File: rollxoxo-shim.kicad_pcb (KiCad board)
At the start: 4 copper layers, 29 x 42 mm, 68 parts, among them J1 USB_C_Receptacle_USB2.0_14P, J2 Conn_01x02, J3 Conn_01x10, J4 Conn_01x01, J5 Conn_01x10, J6 Conn_01x03, J7 Conn_01x01, SW1 SW_Push, SW2 SW_Push, U1 SN74LV1T125DBV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

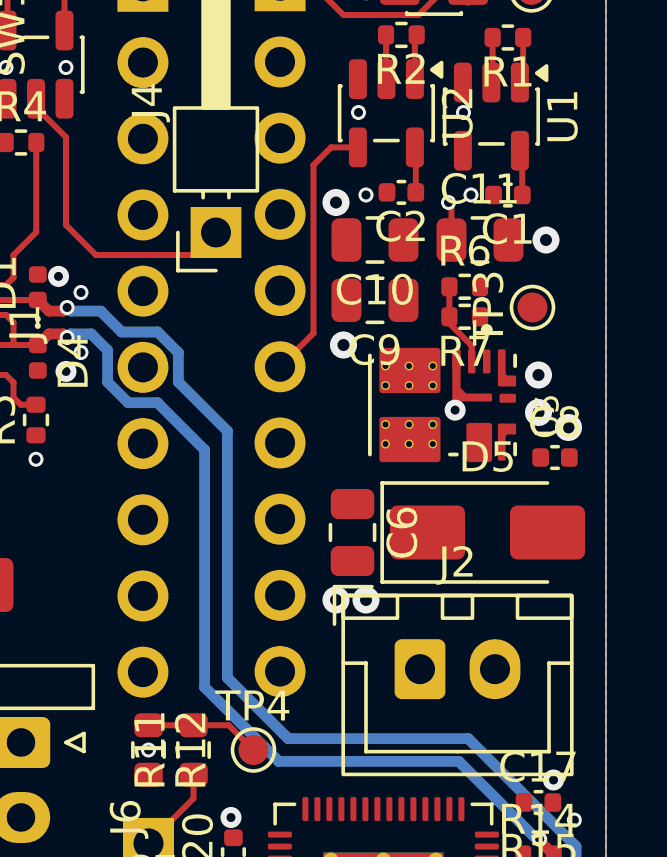
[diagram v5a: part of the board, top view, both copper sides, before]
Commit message: pcb: add power module routing
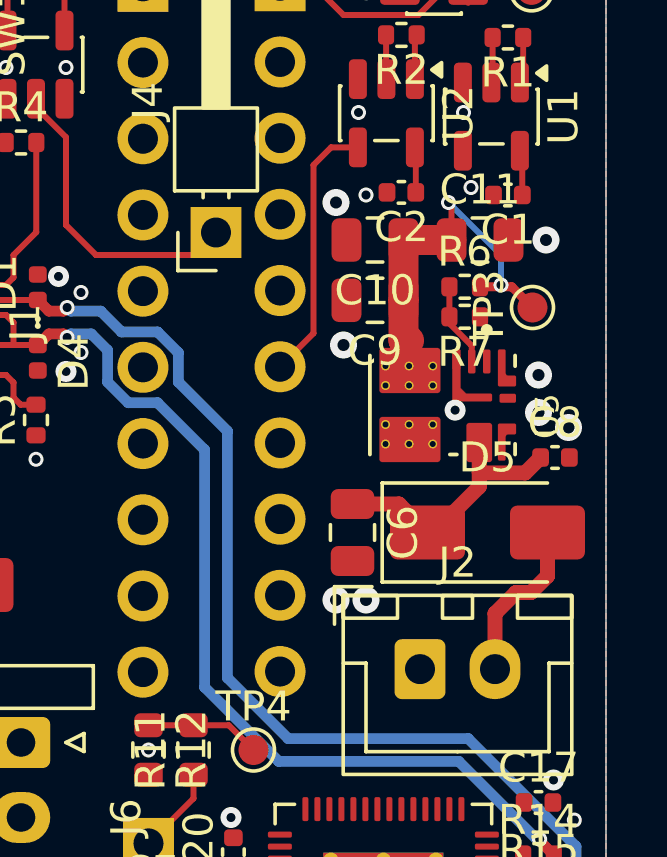
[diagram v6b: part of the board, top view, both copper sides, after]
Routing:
- net +3V3: track 7.66 -> 18.3 mm, vias 1 -> 2
- net +24V: track 0.00 -> 9.24 mm
- net Net-(D5-A): track 0.00 -> 5.57 mm
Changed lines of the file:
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@@
 	)
 	(via
-		(at 78.5 127.75)
+		(at 78.5 127.5)
 		(size 0.5)
 		(drill 0.3)
@@
 	)
 	(segment
+		(start 79.86 130.81)
+		(end 80.55 131.5)
+		(width 0.3)
+		(layer "F.Cu")
+		(net "+3V3")
+	)
+	(segment
 		(start 79.22 123.96)
 		(end 79.18 124)
@@
 	)
 	(segment
+		(start 76.25 131.26)
+		(end 76.25 132.6)
+		(width 1)
+		(layer "F.Cu")
+		(net "+3V3")
+	)
+	(segment
+		(start 78.8 130.81)
+		(end 79.86 130.81)
+		(width 0.3)
+		(layer "F.Cu")
+		(net "+3V3")
+	)
+	(segment
 		(start 75.3375 120.1625)
 		(end 76.13 120.1625)
@@
 	)
 	(segment
+		(start 76.25 129.25)
+		(end 76.25 131.26)
+		(width 1)
+		(layer "F.Cu")
+		(net "+3V3")
+	)
+	(segment
 		(start 77.85 128.1)
 		(end 77.75 128)
@@
 	)
 	(segment
+		(start 76.25 132.6)
+		(end 76.437 132.6)
+		(width 1)
+		(layer "F.Cu")
+		(net "+3V3")
+	)
+	(segment
+		(start 76.25 129.25)
+		(end 77.85 129.25)
+		(width 1)
+		(layer "F.Cu")
+		(net "+3V3")
+	)
+	(segment
 		(start 79.22 122.5)
 		(end 79.22 123.96)
@@
 		(net "+3V3")
 	)
+	(via
+		(at 79.5 130.75)
+		(size 0.5)
+		(drill 0.3)
+		(layers "F.Cu" "B.Cu")
+		(net "+3V3")
+	)
+	(segment
+		(start 79.5 129.75)
+		(end 79.5 130.75)
+		(width 0.2)
+		(layer "B.Cu")
+		(net "+3V3")
+	)
+	(segment
+		(start 77.75 128)
+		(end 79.5 129.75)
+		(width 0.2)
+		(layer "B.Cu")
+		(net "+3V3")
+	)
 	(segment
 		(start 65 128.75)
@@
 	)
 	(segment
+		(start 78.775 135.75)
+		(end 78.775 137)
+		(width 0.5)
+		(layer "F.Cu")
+		(net "+24V")
+	)
+	(segment
+		(start 80.305 137.015)
+		(end 80.82 136.5)
+		(width 0.5)
+		(layer "F.Cu")
+		(net "+24V")
+	)
+	(segment
+		(start 74.55 138.05)
+		(end 76.1 138.05)
+		(width 0.5)
+		(layer "F.Cu")
+		(net "+24V")
+	)
+	(segment
+		(start 78.775 137)
+		(end 78.79 137.015)
+		(width 0.5)
+		(layer "F.Cu")
+		(net "+24V")
+	)
+	(segment
+		(start 76.1 138.05)
+		(end 77.05 139)
+		(width 0.5)
+		(layer "F.Cu")
+		(net "+24V")
+	)
+	(segment
+		(start 78.79 137.015)
+		(end 80.305 137.015)
+		(width 0.5)
+		(layer "F.Cu")
+		(net "+24V")
+	)
+	(segment
+		(start 77.25 139)
+		(end 77.05 139)
+		(width 0.5)
+		(layer "F.Cu")
+		(net "+24V")
+	)
+	(segment
+		(start 78.775 137)
+		(end 78.775 137.475)
+		(width 0.5)
+		(layer "F.Cu")
+		(net "+24V")
+	)
+	(segment
+		(start 78.775 137.475)
+		(end 77.25 139)
+		(width 0.5)
+		(layer "F.Cu")
+		(net "+24V")
+	)
+	(segment
+		(start 80 141)
+		(end 80.5 141)
+		(width 0.5)
+		(layer "F.Cu")
+		(net "Net-(D5-A)")
+	)
+	(segment
+		(start 81.05 140.45)
+		(end 80.5 141)
+		(width 0.5)
+		(layer "F.Cu")
+		(net "Net-(D5-A)")
+	)
+	(segment
+		(start 81.05 139)
+		(end 81.05 140.45)
+		(width 0.5)
+		(layer "F.Cu")
+		(net "Net-(D5-A)")
+	)
+	(segment
+		(start 79.3 143.555)
+		(end 79.3 141.7)
+		(width 0.5)
+		(layer "F.Cu")
+		(net "Net-(D5-A)")
+	)
+	(segment
+		(start 79.3 141.7)
+		(end 80 141)
+		(width 0.5)
+		(layer "F.Cu")
+		(net "Net-(D5-A)")
+	)
+	(segment

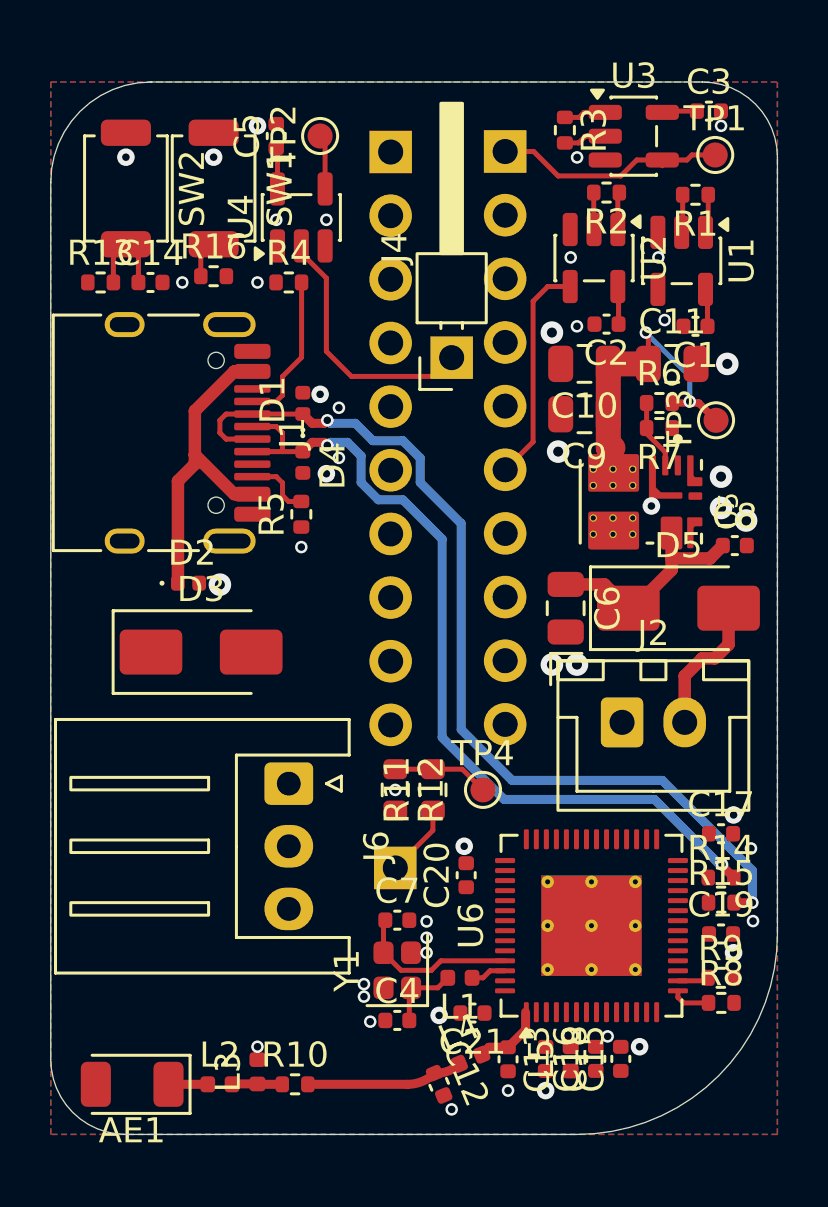
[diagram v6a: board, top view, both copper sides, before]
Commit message: pcb: add +3v3 pwr routing
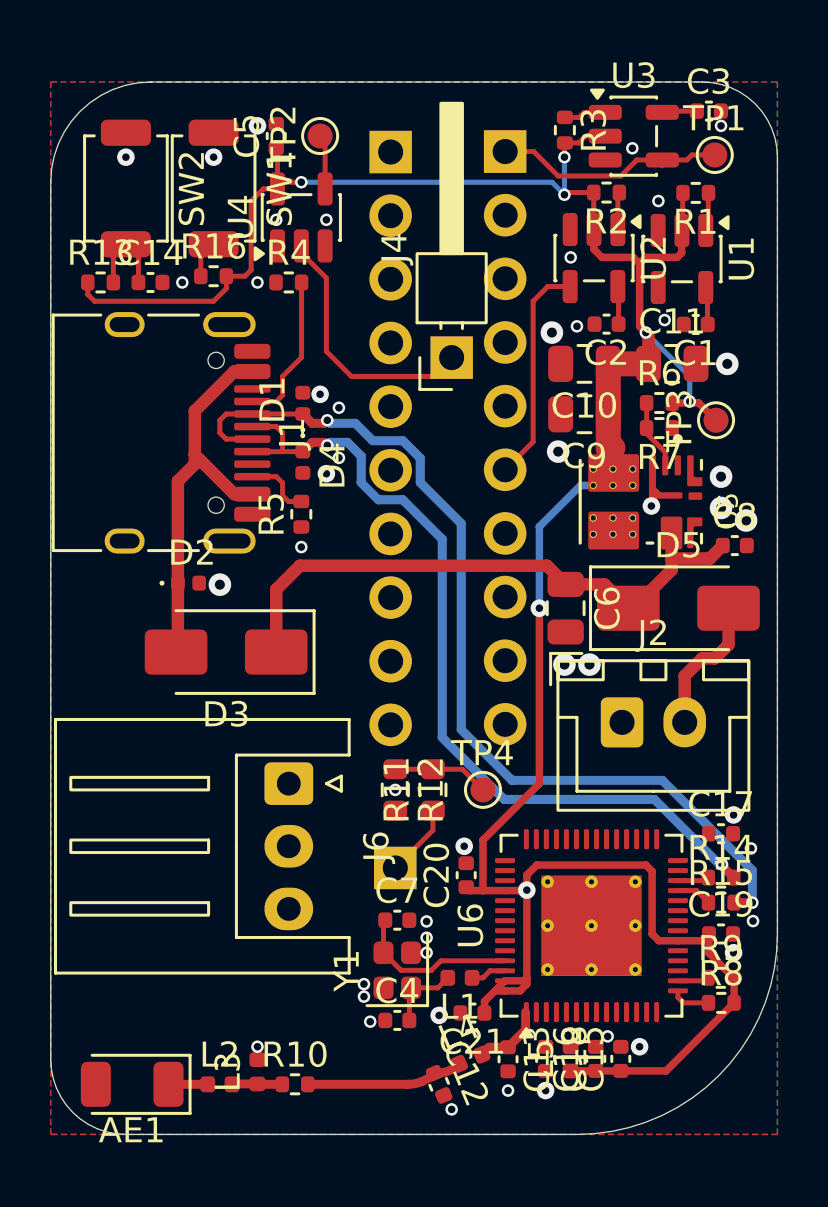
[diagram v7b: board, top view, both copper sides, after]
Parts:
- moved D3 1.00 mm to (61.0, 140.8), turned to 180 degrees
- moved C1 0.07 mm to (79.7, 127.7)
- moved R1 0.07 mm to (79.7, 122.4)
- moved U1 0.07 mm to (79.2, 125.1)
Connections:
- U5 pad 4_1: (no net) -> +3V3
- U5 pad 4_2: (no net) -> +3V3
- U5 pad 4_3: (no net) -> +3V3
- U5 pad 4_4: (no net) -> +3V3
- U5 pad 4_5: (no net) -> +3V3
- U5 pad 4_6: (no net) -> +3V3
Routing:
- net +3V3: track 18.3 -> 103.8 mm, vias 2 -> 7
- net +24V: track 9.24 -> 24.0 mm
- net +Vbus: track 13.0 -> 15.8 mm
- net /ESP_D-: track 0.00 -> 1.42 mm
- net /ESP_D+: track 0.00 -> 1.26 mm

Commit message: pcb: add through routing
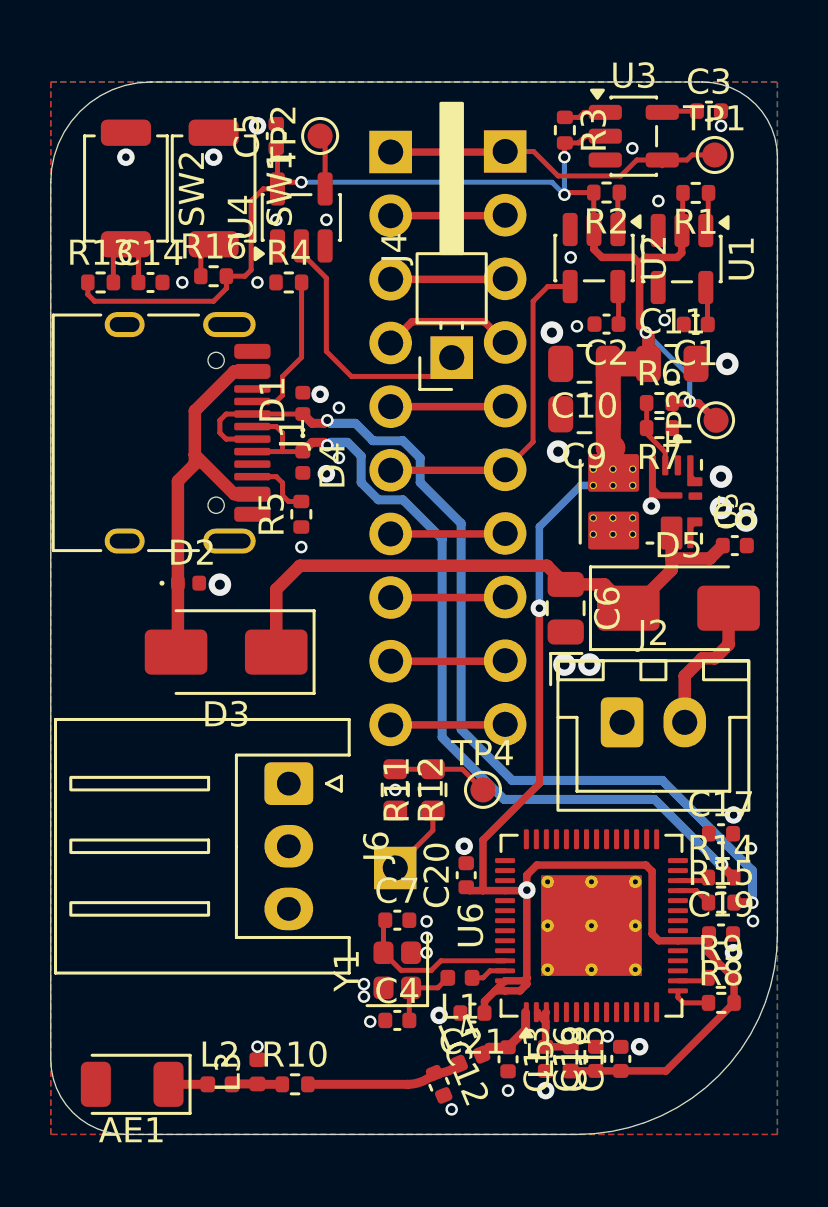
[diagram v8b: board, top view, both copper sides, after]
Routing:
- net Net-(J3-Pin_4): track 0.00 -> 5.27 mm
- net /STOP_BTN: track 8.91 -> 13.5 mm
- net Net-(J3-Pin_9): track 0.00 -> 4.58 mm
- net Net-(J3-Pin_5): track 0.00 -> 4.58 mm
- net /DOWN_BTN: track 0.00 -> 4.58 mm
- net +5V: track 4.42 -> 9.00 mm
- net Net-(J3-Pin_3): track 0.00 -> 4.58 mm
- net Net-(J3-Pin_2): track 0.00 -> 4.58 mm
- net /UP_BTN: track 9.37 -> 13.9 mm
- net Net-(J3-Pin_8): track 0.00 -> 4.58 mm
- net VDD3P3: track 0.00 -> 3.16 mm
